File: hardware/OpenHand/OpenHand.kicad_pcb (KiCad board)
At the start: 4 copper layers, 110 x 50 mm, 214 parts, among them J1 CONN_MOTOR_1, J10 CONN_FDBK_2, J11 CONN_EMG_2, J12 CONN_POS_3, J2 CONN_MOTOR_2, J3 CONN_BATT, J4 CONN_POS_1, J5 USB_C_CONN, J6 CONN_MOTOR_3, J7 CONN_FDBK_1, J8 CONN_EMG_1, J9 CONN_POS_2, Q1 AO3401A, SW1 BTN_RST, SW2 BTN_BOOT, SW3 SW_Push, U1 STM32F103RETx, U10 DRV8833PWP, U2 TPS565201DDCR, U3 AMS1117-3.3, U4 LT1175-5_SOT223, U5 LM324, U6 LM324, U7 DRV8833PWP, U8 DRV8833PWP, U9 DRV8833PWP

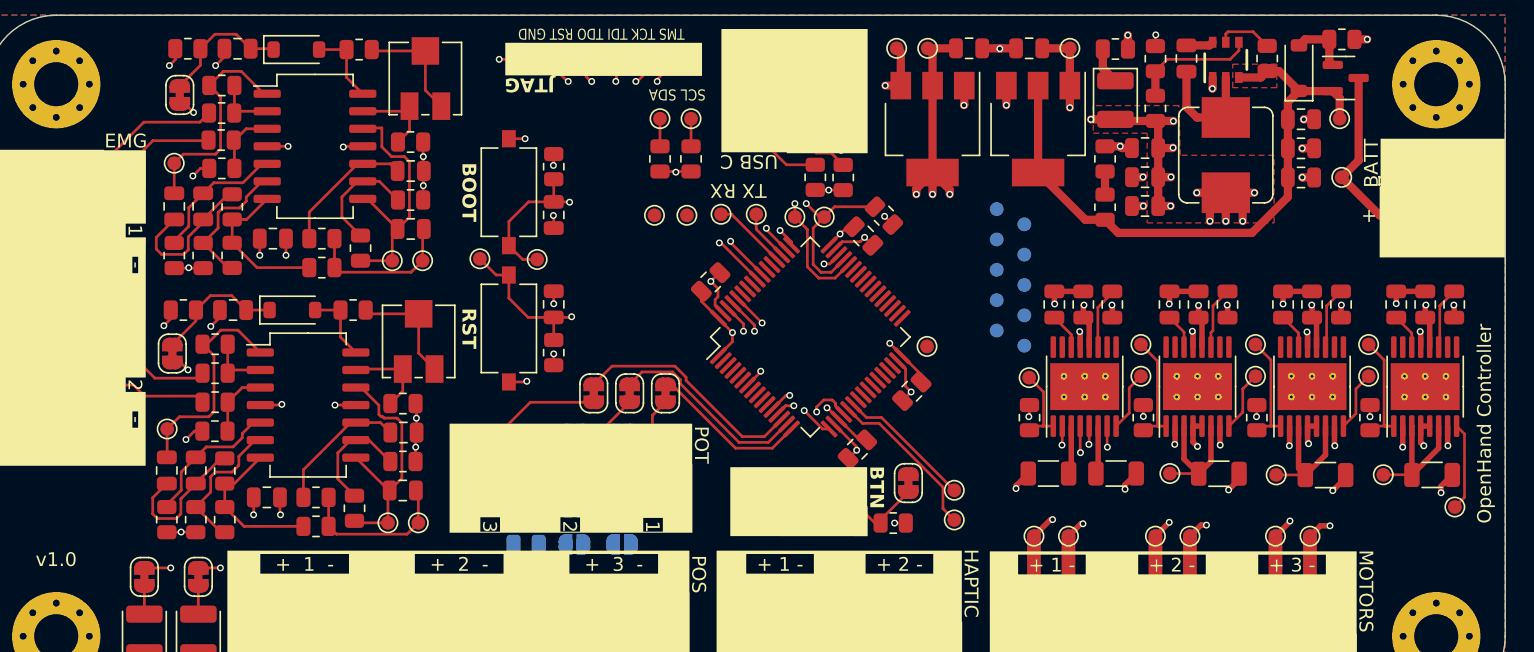
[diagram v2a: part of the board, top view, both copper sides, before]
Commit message: Update PCB and order it from JLCPCB
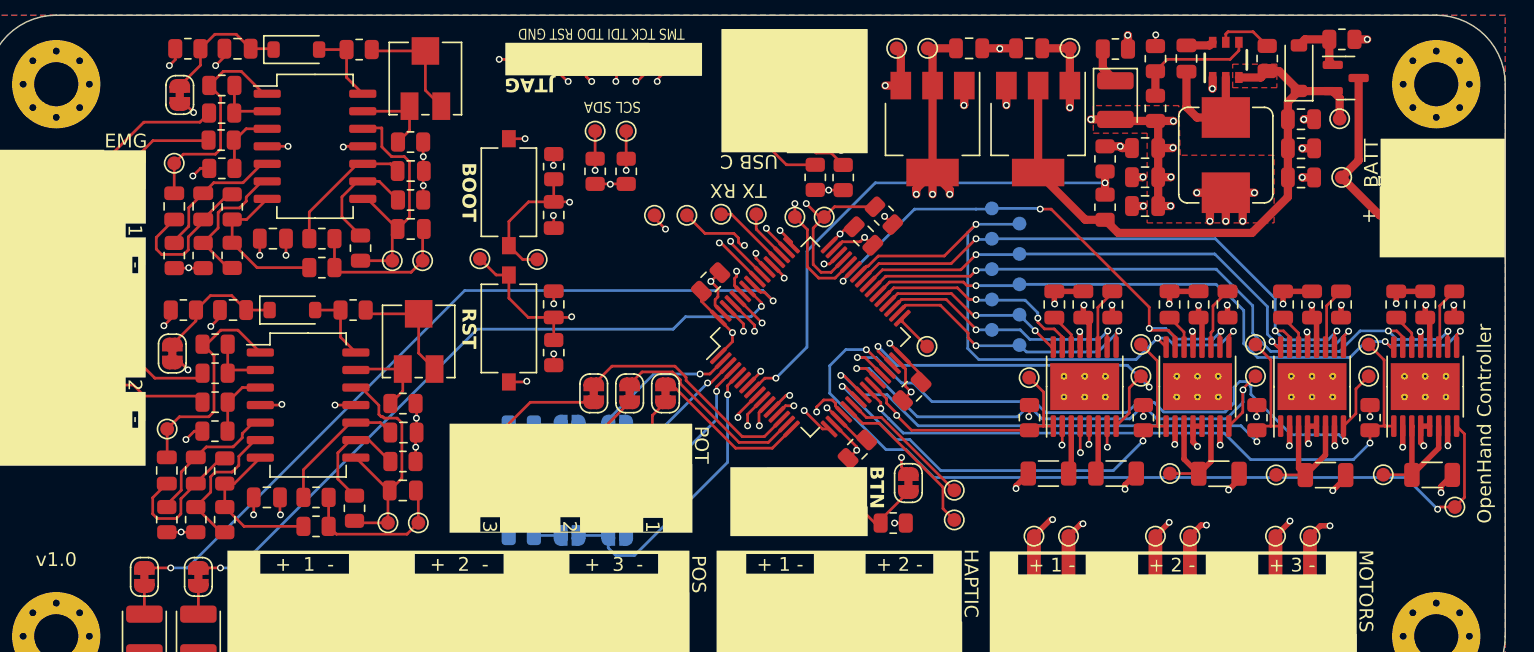
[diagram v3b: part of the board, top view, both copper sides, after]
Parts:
- moved R6 4.79 mm to (144.1, 111.3)
- moved R7 4.79 mm to (146.3, 111.3)
- moved TP21 4.79 mm to (146.3, 108.4)
- moved TP22 4.79 mm to (144.1, 108.4)
- moved JP10 0.74 mm to (142.2, 137.7)
- moved JP7 0.74 mm to (142.2, 129.7)
- moved JP8 0.74 mm to (142.2, 132.3)
- moved JP9 0.74 mm to (142.2, 135.0)
- moved R13 0.74 mm to (138.7, 129.7)
- moved R14 0.74 mm to (138.7, 132.3)
- moved R15 0.74 mm to (138.7, 135.0)
- moved R16 0.74 mm to (138.7, 137.7)
- moved JP11 0.74 mm to (145.7, 129.7)
- moved JP12 0.74 mm to (145.7, 132.3)
- moved JP13 0.74 mm to (145.7, 135.0)
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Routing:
- net MOTOR_03_FAULT: track 6.39 -> 62.5 mm, vias 0 -> 2
- net LED_1: track 1.91 -> 56.2 mm, vias 1 -> 2
- net MOTOR_03_PWM: track 0.00 -> 50.6 mm, vias 0 -> 3
- net MOTOR_03_DIR: track 0.00 -> 49.9 mm, vias 0 -> 3
- net LED_2: track 1.60 -> 50.3 mm, vias 1 -> 2
- net MOTOR_01_DIR: track 0.00 -> 45.8 mm, vias 0 -> 3
- net MOTOR_02_FAULT: track 4.37 -> 49.2 mm, vias 0 -> 2
- net MOTOR_02_PWM: track 0.00 -> 43.8 mm, vias 0 -> 3
- net MOTOR_02_DIR: track 0.00 -> 42.6 mm, vias 0 -> 3
- net MOTOR_03_EN: track 8.25 -> 48.5 mm, vias 0 -> 2
- net MOTOR_01_PWM: track 0.00 -> 40.2 mm, vias 0 -> 4
- net HALL_SENS_01_S: track 0.00 -> 40.2 mm, vias 0 -> 1
- net /BATT_SENSE: track 1.67 -> 37.5 mm, vias 0 -> 2
- net MOTOR_02_EN: track 8.23 -> 43.3 mm, vias 0 -> 2
- net MOTOR_01_FAULT: track 4.41 -> 38.3 mm, vias 0 -> 2
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
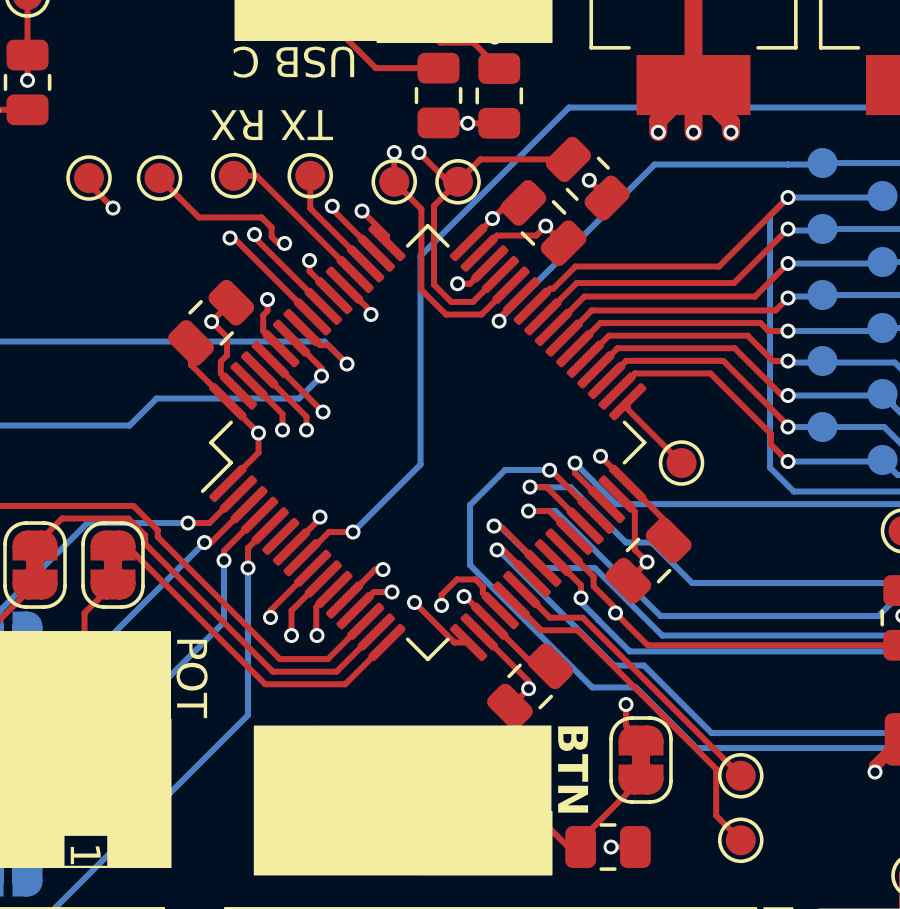
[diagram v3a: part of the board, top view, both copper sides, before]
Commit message: Update to KiCAD 8 and order components from LCSC
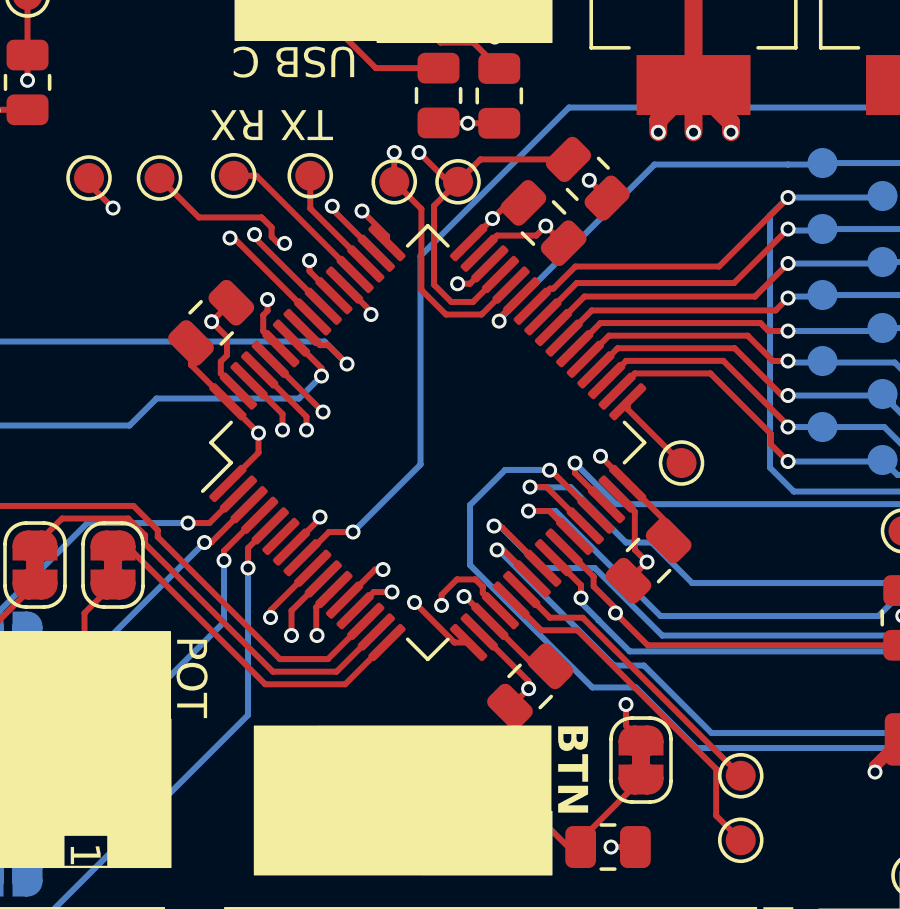
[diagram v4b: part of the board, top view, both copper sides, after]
